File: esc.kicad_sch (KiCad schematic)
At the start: 72 parts, among them J8 Conn_01x04, Q10 NMOS, Q5 NMOS, Q6 NMOS, Q7 NMOS, Q8 NMOS, Q9 NMOS, U15 STM32G071K8U6, U16 DRV8328ARUYR, U7 INA190A3IDCKR

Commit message: ESC mostly done apart from STM routing
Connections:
- net VSENSE_REF: now also U15.10 (PA3); no longer U15.8 (PA1)
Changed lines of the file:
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@@
+	)
+	(no_connect
+		(at 49.53 55.88)
 	)
 	(no_connect
@@
 	)
 	(no_connect
-		(at 49.53 60.96)
-	)
-	(no_connect
 		(at 99.06 58.42)
 	)
@@
 	(wire
 		(pts
-			(xy 46.99 55.88) (xy 49.53 55.88)
-		)
-		(stroke
-			(width 0)
-			(type default)
-		)
-	)
-	(wire
-		(pts
 			(xy 234.95 147.32) (xy 246.38 147.32)
 		)
@@
 		)
 	)
+	(label "VSENSE_REF"
+		(at 49.53 60.96 180)
+		(effects
+			(font
+				(size 1.27 1.27)
+			)
+			(justify right bottom)
+		)
+	)
 	(label "GHC"
 		(at 238.76 33.02 0)
@@
 		)
 	)
-	(label "VSENSE_REF"
-		(at 46.99 55.88 180)
-		(effects
-			(font
-				(size 1.27 1.27)
-			)
-			(justify right bottom)
-		)
-	)

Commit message: Done routing for first ESC version
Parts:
- removed TP19: TestPoint, easyeda2kicad:TestPoint_Pad_D1.0mm_No_Courtyard, symbol Connector:TestPoint
- added C198, C202, C206: 10u, Capacitor_SMD:C_1206_3216Metric, symbol Device:C
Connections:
- net +BATT: now also C198.2, C202.2, C206.2
- net GND: now also C198.1, C202.1, C206.1
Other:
- moved on the sheet: C112, C113, C114, C115, C116, C118, C120, C121, C122, C123, C124, C125

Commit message: Improve ESC V2 routing
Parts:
- C102, C105: footprint Capacitor_SMD:C_1206_3216Metric -> Capacitor_SMD:C_0805_2012Metric
- C103: footprint Capacitor_SMD:C_0603_1608Metric -> Capacitor_SMD:C_0402_1005Metric
- C109, C110, C111: footprint Capacitor_SMD:C_0805_2012Metric -> Capacitor_SMD:C_0603_1608Metric
- R69, R70, R73, R74, R81, R82: footprint Resistor_SMD:R_0603_1608Metric -> Resistor_SMD:R_0201_0603Metric
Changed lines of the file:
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@@
 			)
 		)
-		(property "Footprint" "Resistor_SMD:R_0603_1608Metric"
+		(property "Footprint" "Resistor_SMD:R_0201_0603Metric"
 			(at 200.66 46.482 90)
 			(hide yes)
@@
 			)
 		)
-		(property "Footprint" "Resistor_SMD:R_0603_1608Metric"
+		(property "Footprint" "Resistor_SMD:R_0201_0603Metric"
 			(at 200.66 31.242 90)
 			(hide yes)
@@
 			)
 		)
-		(property "Footprint" "Capacitor_SMD:C_0805_2012Metric"
+		(property "Footprint" "Capacitor_SMD:C_0603_1608Metric"
 			(at 99.06 144.4752 0)
 			(hide yes)
@@
 			)
 		)
-		(property "Footprint" "Capacitor_SMD:C_0603_1608Metric"
+		(property "Footprint" "Capacitor_SMD:C_0402_1005Metric"
 			(at 32.0548 144.78 0)
 			(hide yes)
@@
 			)
 		)
-		(property "Footprint" "Capacitor_SMD:C_1206_3216Metric"
+		(property "Footprint" "Capacitor_SMD:C_0805_2012Metric"
 			(at 20.6248 144.78 0)
 			(hide yes)
@@
 			)
 		)
-		(property "Footprint" "Resistor_SMD:R_0603_1608Metric"
+		(property "Footprint" "Resistor_SMD:R_0201_0603Metric"
 			(at 154.94 31.242 90)
 			(hide yes)
@@
 			)
 		)
-		(property "Footprint" "Resistor_SMD:R_0603_1608Metric"
+		(property "Footprint" "Resistor_SMD:R_0201_0603Metric"
 			(at 246.38 46.482 90)
 			(hide yes)
@@
 			)
 		)
-		(property "Footprint" "Capacitor_SMD:C_0805_2012Metric"
+		(property "Footprint" "Capacitor_SMD:C_0603_1608Metric"
 			(at 99.06 136.8552 0)
 			(hide yes)
@@
 			)
 		)
-		(property "Footprint" "Capacitor_SMD:C_0805_2012Metric"
+		(property "Footprint" "Capacitor_SMD:C_0603_1608Metric"
 			(at 99.06 152.0952 0)
 			(hide yes)
@@
 			)
 		)
-		(property "Footprint" "Resistor_SMD:R_0603_1608Metric"
+		(property "Footprint" "Resistor_SMD:R_0201_0603Metric"
 			(at 246.38 31.242 90)
 			(hide yes)
@@
 			)
 		)
-		(property "Footprint" "Capacitor_SMD:C_1206_3216Metric"
+		(property "Footprint" "Capacitor_SMD:C_0805_2012Metric"
 			(at 47.2948 144.78 0)
 			(hide yes)
@@
 			)
 		)
-		(property "Footprint" "Resistor_SMD:R_0603_1608Metric"
+		(property "Footprint" "Resistor_SMD:R_0201_0603Metric"
 			(at 154.94 46.482 90)
 			(hide yes)

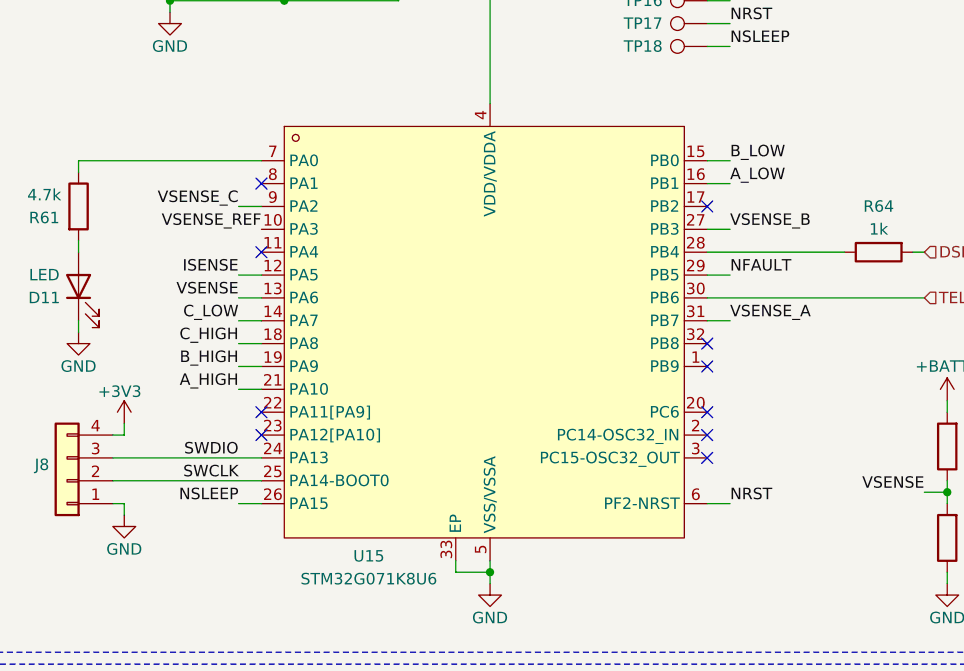
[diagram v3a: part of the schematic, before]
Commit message: Finish initial ESC V2 layout
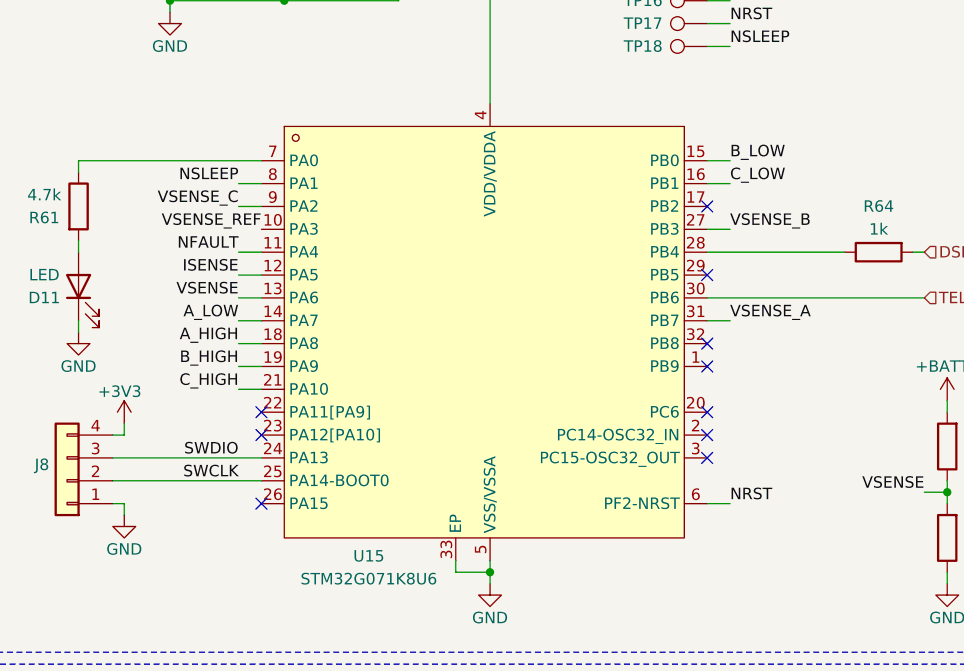
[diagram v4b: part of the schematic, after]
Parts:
- R61, R62, R63, R64, R65, R66, R67, R68, R75, R76, R77, R78, R79, R80, R83, R84, R85: footprint Resistor_SMD:R_0402_1005Metric -> Resistor_SMD:R_0201_0603Metric
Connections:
- net A_HIGH: now also U15.18 (PA8); no longer U15.21 (PA10)
- net A_LOW: now also U15.14 (PA7); no longer U15.16 (PB1)
- net C_HIGH: now also U15.21 (PA10); no longer U15.18 (PA8)
- net C_LOW: now also U15.16 (PB1); no longer U15.14 (PA7)
- net NFAULT: now also U15.11 (PA4); no longer U15.29 (PB5)
- net NSLEEP: now also U15.8 (PA1); no longer U15.26 (PA15)
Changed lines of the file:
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@@
 	)
 	(no_connect
-		(at 99.06 83.82)
+		(at 49.53 91.44)
 	)
 	(no_connect
-		(at 49.53 55.88)
+		(at 99.06 83.82)
 	)
 	(no_connect
@@
 	)
 	(no_connect
-		(at 49.53 63.5)
+		(at 99.06 81.28)
 	)
 	(no_connect
-		(at 99.06 81.28)
+		(at 99.06 66.04)
 	)
 	(no_connect
@@
 	(wire
 		(pts
-			(xy 46.99 91.44) (xy 49.53 91.44)
-		)
-		(stroke
-			(width 0)
-			(type default)
-		)
-	)
-	(wire
-		(pts
 			(xy 270.51 120.65) (xy 279.4 120.65)
 		)
@@
 	(wire
 		(pts
+			(xy 46.99 55.88) (xy 49.53 55.88)
+		)
+		(stroke
+			(width 0)
+			(type default)
+		)
+	)
+	(wire
+		(pts
 			(xy 93.98 160.02) (xy 91.44 160.02)
 		)
@@
 	(wire
 		(pts
-			(xy 29.21 71.12) (xy 29.21 72.39)
+			(xy 46.99 63.5) (xy 49.53 63.5)
 		)
 		(stroke
@@
 	(wire
 		(pts
-			(xy 158.75 33.02) (xy 160.02 33.02)
+			(xy 29.21 71.12) (xy 29.21 72.39)
 		)
 		(stroke
@@
 	(wire
 		(pts
-			(xy 167.64 57.15) (xy 259.08 57.15)
+			(xy 158.75 33.02) (xy 160.02 33.02)
 		)
 		(stroke
@@
 	(wire
 		(pts
-			(xy 161.29 147.32) (xy 172.72 147.32)
+			(xy 167.64 57.15) (xy 259.08 57.15)
 		)
 		(stroke
@@
 	(wire
 		(pts
-			(xy 261.62 134.62) (xy 261.62 135.89)
+			(xy 161.29 147.32) (xy 172.72 147.32)
 		)
 		(stroke
@@
 	(wire
 		(pts
-			(xy 129.54 130.81) (xy 129.54 129.54)
+			(xy 261.62 134.62) (xy 261.62 135.89)
 		)
 		(stroke
@@
 	(wire
 		(pts
-			(xy 261.62 105.41) (xy 261.62 106.68)
+			(xy 129.54 130.81) (xy 129.54 129.54)
 		)
 		(stroke
@@
 	(wire
 		(pts
-			(xy 184.15 120.65) (xy 195.58 120.65)
+			(xy 261.62 105.41) (xy 261.62 106.68)
 		)
 		(stroke
@@
 	(wire
 		(pts
-			(xy 101.6 66.04) (xy 99.06 66.04)
+			(xy 184.15 120.65) (xy 195.58 120.65)
 		)
 		(stroke
@@
 		)
 	)
+	(label "C_LOW"
+		(at 101.6 55.88 0)
+		(effects
+			(font
+				(size 1.27 1.27)
+			)
+			(justify left bottom)
+		)
+	)
 	(label "A_LOW"
 		(at 63.5 160.02 180)
@@
 		)
 	)
-	(label "A_LOW"
-		(at 101.6 55.88 0)
-		(effects
-			(font
-				(size 1.27 1.27)
-			)
-			(justify left bottom)
-		)
-	)
 	(label "GLA"
 		(at 93.98 160.02 0)
@@
 		)
 	)
-	(label "C_HIGH"
-		(at 46.99 73.66 180)
-		(effects
-			(font
-				(size 1.27 1.27)
-			)
-			(justify right bottom)
-		)
-	)
 	(label "VSENSE_C"
 		(at 250.19 120.65 0)
@@
 		)
 	)
-	(label "A_HIGH"
-		(at 46.99 78.74 180)
+	(label "GHB"
+		(at 193.04 33.02 0)
 		(effects
 			(font
 				(size 1.27 1.27)
 			)
-			(justify right bottom)
+			(justify left bottom)
 		)
 	)
-	(label "GHB"
-		(at 193.04 33.02 0)
+	(label "GLA"
+		(at 147.32 48.26 0)
 		(effects
 			(font
@@
 		)
 	)
-	(label "GLA"
-		(at 147.32 48.26 0)
+	(label "A_HIGH"
+		(at 46.99 73.66 180)
 		(effects
 			(font
 				(size 1.27 1.27)
 			)
-			(justify left bottom)
+			(justify right bottom)
 		)
 	)
@@
 		)
 	)
+	(label "C_HIGH"
+		(at 46.99 78.74 180)
+		(effects
+			(font
+				(size 1.27 1.27)
+			)
+			(justify right bottom)
+		)
+	)
 	(label "B_HIGH"
 		(at 46.99 76.2 180)
@@
 	)
 	(label "NSLEEP"
-		(at 46.99 91.44 180)
-		(effects
-			(font
-				(size 1.27 1.27)
-			)
-			(justify right bottom)
-		)
-	)
-	(label "NFAULT"
-		(at 101.6 66.04 0)
-		(effects
-			(font
-				(size 1.27 1.27)
-			)
-			(justify left bottom)
-		)
-	)
-	(label "C_LOW"
-		(at 46.99 71.12 180)
-		(effects
-			(font
-				(size 1.27 1.27)
-			)
-			(justify right bottom)
-		)
-	)
-	(label "NSLEEP"
 		(at 63.5 151.13 180)
 		(effects
@@
 		)
 	)
+	(label "NFAULT"
+		(at 46.99 63.5 180)
+		(effects
+			(font
+				(size 1.27 1.27)
+			)
+			(justify right bottom)
+		)
+	)
+	(label "NSLEEP"
+		(at 46.99 55.88 180)
+		(effects
+			(font
+				(size 1.27 1.27)
+			)
+			(justify right bottom)
+		)
+	)
 	(label "NSLEEP"
 		(at 101.6 40.64 0)
@@
 		)
 	)
+	(label "A_LOW"
+		(at 46.99 71.12 180)
+		(effects
+			(font
+				(size 1.27 1.27)
+			)
+			(justify right bottom)
+		)
+	)
 	(label "PHASE_C"
 		(at 110.49 154.94 0)
@@
 			)
 		)
-		(property "Footprint" "Resistor_SMD:R_0402_1005Metric"
+		(property "Footprint" "Resistor_SMD:R_0201_0603Metric"
 			(at 266.7 118.872 90)
 			(hide yes)
@@
 			)
 		)
-		(property "Footprint" "Resistor_SMD:R_0402_1005Metric"
+		(property "Footprint" "Resistor_SMD:R_0201_0603Metric"
 			(at 230.378 130.81 90)
 			(hide yes)
@@
 			)
 		)
-		(property "Footprint" "Resistor_SMD:R_0402_1005Metric"
+		(property "Footprint" "Resistor_SMD:R_0201_0603Metric"
 			(at 230.378 110.49 90)
 			(hide yes)
@@
 			)
 		)
-		(property "Footprint" "Resistor_SMD:R_0402_1005Metric"
+		(property "Footprint" "Resistor_SMD:R_0201_0603Metric"
 			(at 197.358 130.81 90)
 			(hide yes)
@@
 			)
 		)
-		(property "Footprint" "Resistor_SMD:R_0402_1005Metric"
+		(property "Footprint" "Resistor_SMD:R_0201_0603Metric"
 			(at 263.398 110.49 90)
 			(hide yes)
@@
 			)
 		)
-		(property "Footprint" "Resistor_SMD:R_0402_1005Metric"
+		(property "Footprint" "Resistor_SMD:R_0201_0603Metric"
 			(at 197.358 110.49 90)
 			(hide yes)
@@
 			)
 		)
-		(property "Footprint" "Resistor_SMD:R_0402_1005Metric"
+		(property "Footprint" "Resistor_SMD:R_0201_0603Metric"
 			(at 127.508 95.25 90)
 			(hide yes)
@@
 			)
 		)
-		(property "Footprint" "Resistor_SMD:R_0402_1005Metric"
+		(property "Footprint" "Resistor_SMD:R_0201_0603Metric"
 			(at 97.028 123.19 90)
 			(hide yes)
@@
 			)
 		)
-		(property "Footprint" "Resistor_SMD:R_0402_1005Metric"
+		(property "Footprint" "Resistor_SMD:R_0201_0603Metric"
 			(at 131.318 135.89 90)
 			(hide yes)
@@
 			)
 		)
-		(property "Footprint" "Resistor_SMD:R_0402_1005Metric"
+		(property "Footprint" "Resistor_SMD:R_0201_0603Metric"
 			(at 127.508 85.09 90)
 			(hide yes)
@@
 			)
 		)
-		(property "Footprint" "Resistor_SMD:R_0402_1005Metric"
+		(property "Footprint" "Resistor_SMD:R_0201_0603Metric"
 			(at 200.66 118.872 90)
 			(hide yes)
@@
 			)
 		)
-		(property "Footprint" "Resistor_SMD:R_0402_1005Metric"
+		(property "Footprint" "Resistor_SMD:R_0201_0603Metric"
 			(at 233.68 118.872 90)
 			(hide yes)
@@
 			)
 		)
-		(property "Footprint" "Resistor_SMD:R_0402_1005Metric"
+		(property "Footprint" "Resistor_SMD:R_0201_0603Metric"
 			(at 44.45 155.448 90)
 			(hide yes)
@@
 			)
 		)
-		(property "Footprint" "Resistor_SMD:R_0402_1005Metric"
+		(property "Footprint" "Resistor_SMD:R_0201_0603Metric"
 			(at 118.11 61.722 90)
 			(hide yes)
@@
 			)
 		)
-		(property "Footprint" "Resistor_SMD:R_0402_1005Metric"
+		(property "Footprint" "Resistor_SMD:R_0201_0603Metric"
 			(at 131.318 125.73 90)
 			(hide yes)
@@
 			)
 		)
-		(property "Footprint" "Resistor_SMD:R_0402_1005Metric"
+		(property "Footprint" "Resistor_SMD:R_0201_0603Metric"
 			(at 27.432 58.42 90)
 			(hide yes)
@@
 			)
 		)
-		(property "Footprint" "Resistor_SMD:R_0402_1005Metric"
+		(property "Footprint" "Resistor_SMD:R_0201_0603Metric"
 			(at 263.398 130.81 90)
 			(hide yes)

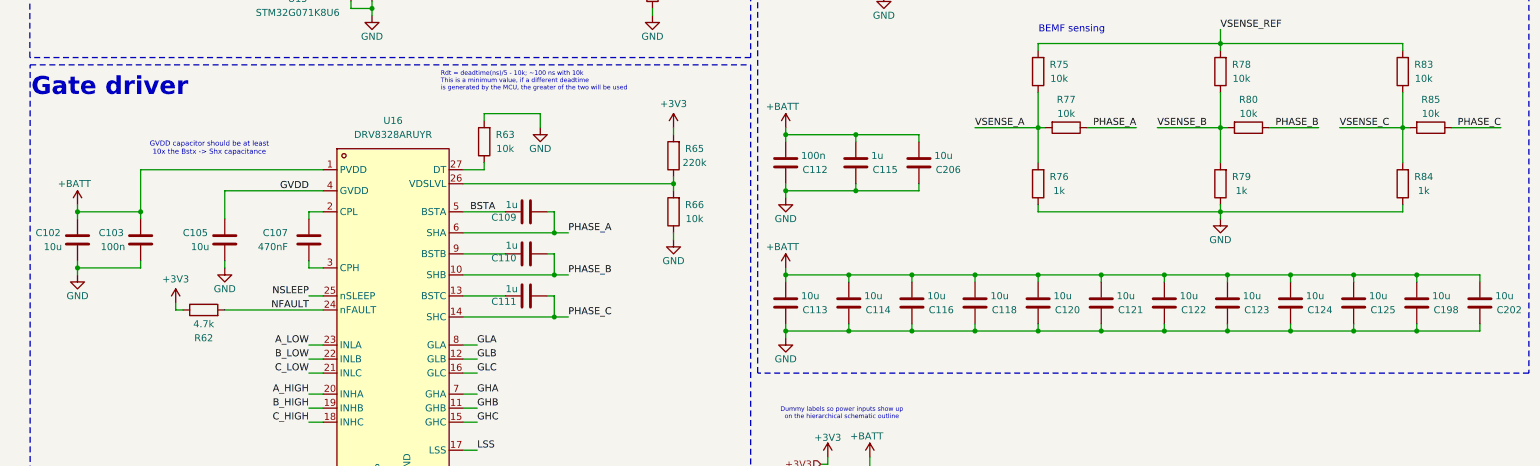
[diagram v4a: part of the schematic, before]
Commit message: Add 3 more caps and remove floating islands in ESC V2
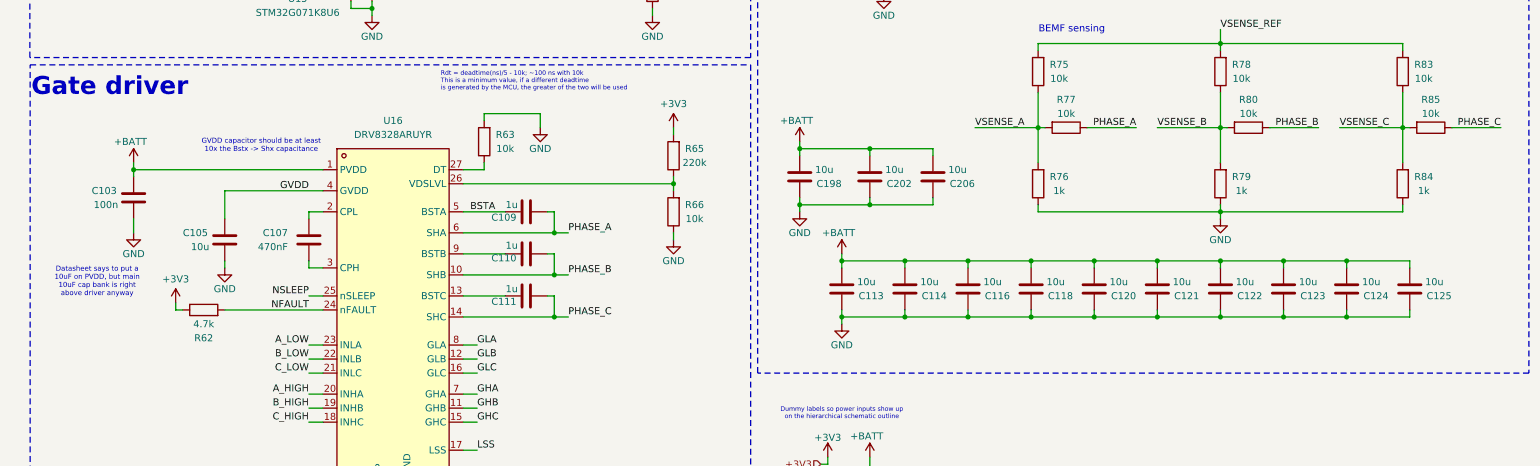
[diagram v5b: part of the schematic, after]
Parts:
- removed C102: 10u, Capacitor_SMD:C_0805_2012Metric, symbol Device:C
- removed C112: 100n, Capacitor_SMD:C_0402_1005Metric, symbol Device:C
- removed C115: 1u, Capacitor_SMD:C_0805_2012Metric, symbol Device:C
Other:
- note added: "Datasheet says to put a 10uF on PVDD, but main 10uF cap bank is right above driver anyway"
- moved on the sheet: C103, C113, C114, C116, C118, C120, C121, C122, C123, C124, C125, C198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
